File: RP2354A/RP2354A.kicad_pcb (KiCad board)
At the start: 2 copper layers, 40 x 80 mm, 66 parts, among them J101 USB4085-GF-A, J102 AudioJack2_SwitchT, J103 AudioJack2_SwitchT, J201 TC2030-NL, SW201 SW_Push_DPDT, U101 OPA365xxDBV, U201 RP2354A, U202 NCP1117-3.3_SOT223, U301 TAC5112, Y201 ABM8-272-T3

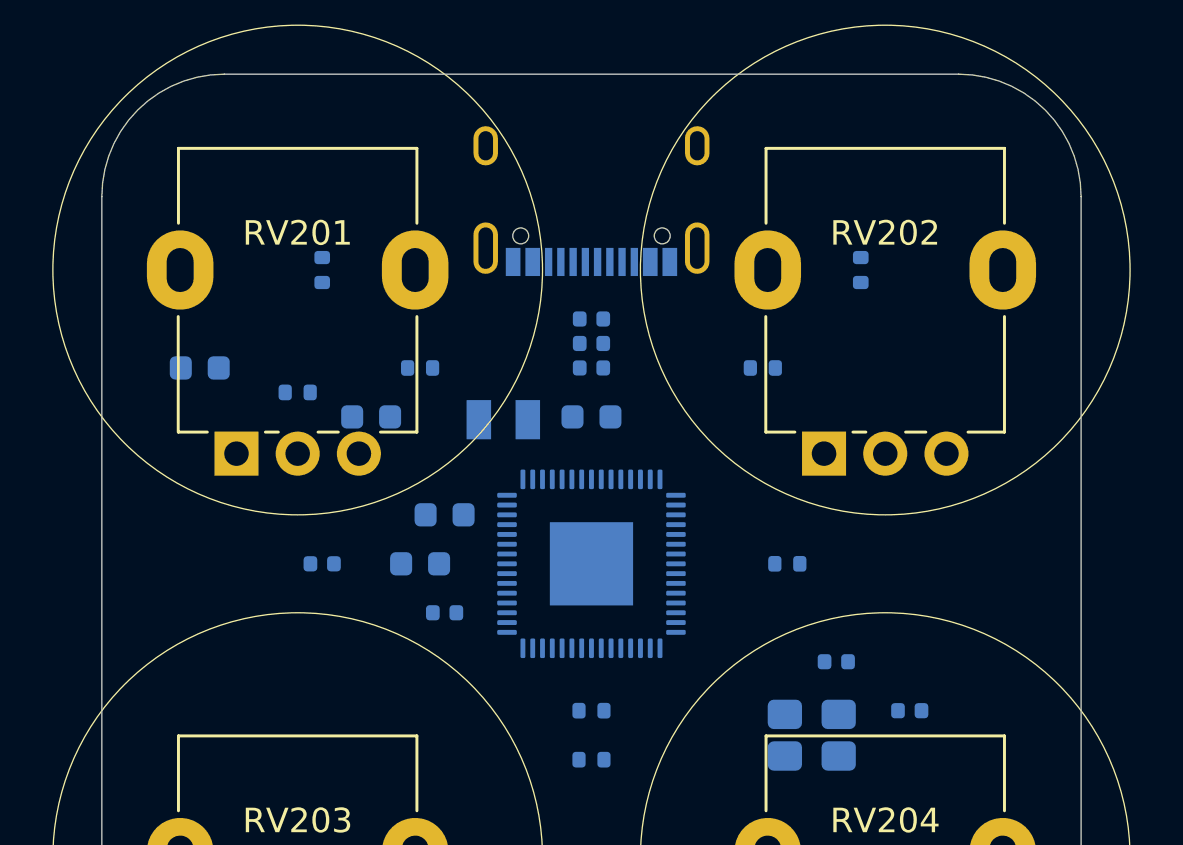
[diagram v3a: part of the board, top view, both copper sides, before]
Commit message: Replace two of the pots with basic ones without mounting pins
... for the most ridiculous of reasons: it frees up some board space
without altering the physical layout of knobs.

I can't replace all the pots with the basic ones, because the pots
themselves are physically bigger and won't fit, but this odd mix of
potentiometer types works, even if it's all kinds of odd.

Does this board need to be this form factor? No.  I could just move
things around.  But I like the size, I like the bigger 20mm diameter
knobs I'm planning on using, and I'm just doing this ridiculous thing
for fun in the first place, so having a fun form factor is part of it
all.

The ridiculous reason for having four knobs in the first place? That's
how many ADCs the RP2354A has. So this is all very random.

Next up: do a 4-layer stackup and actually start laying things out.

Signed-off-by: Linus Torvalds <torvalds@linux-foundation.org>
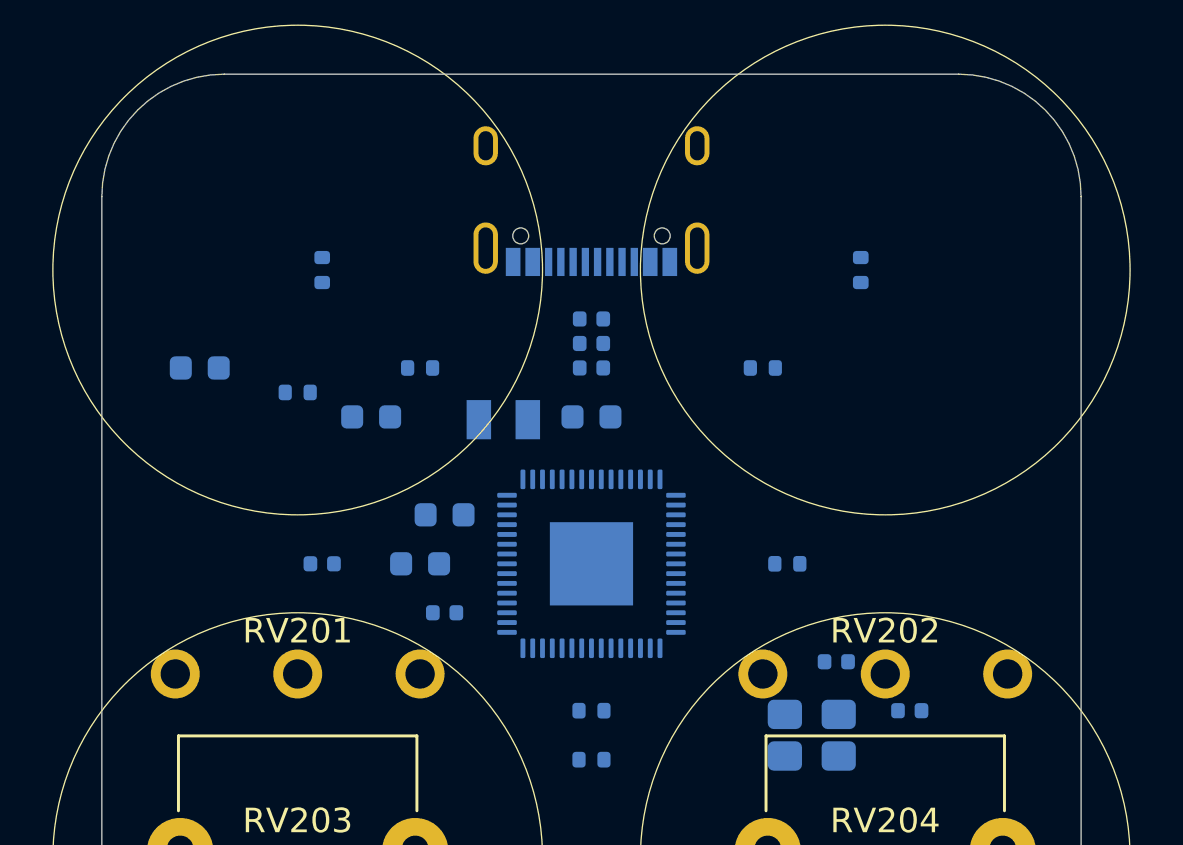
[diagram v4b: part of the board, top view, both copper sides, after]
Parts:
- RV201, RV202: footprint Mylib:Potentiometer_9mm_MP -> Mylib:Potentiometer-Basic

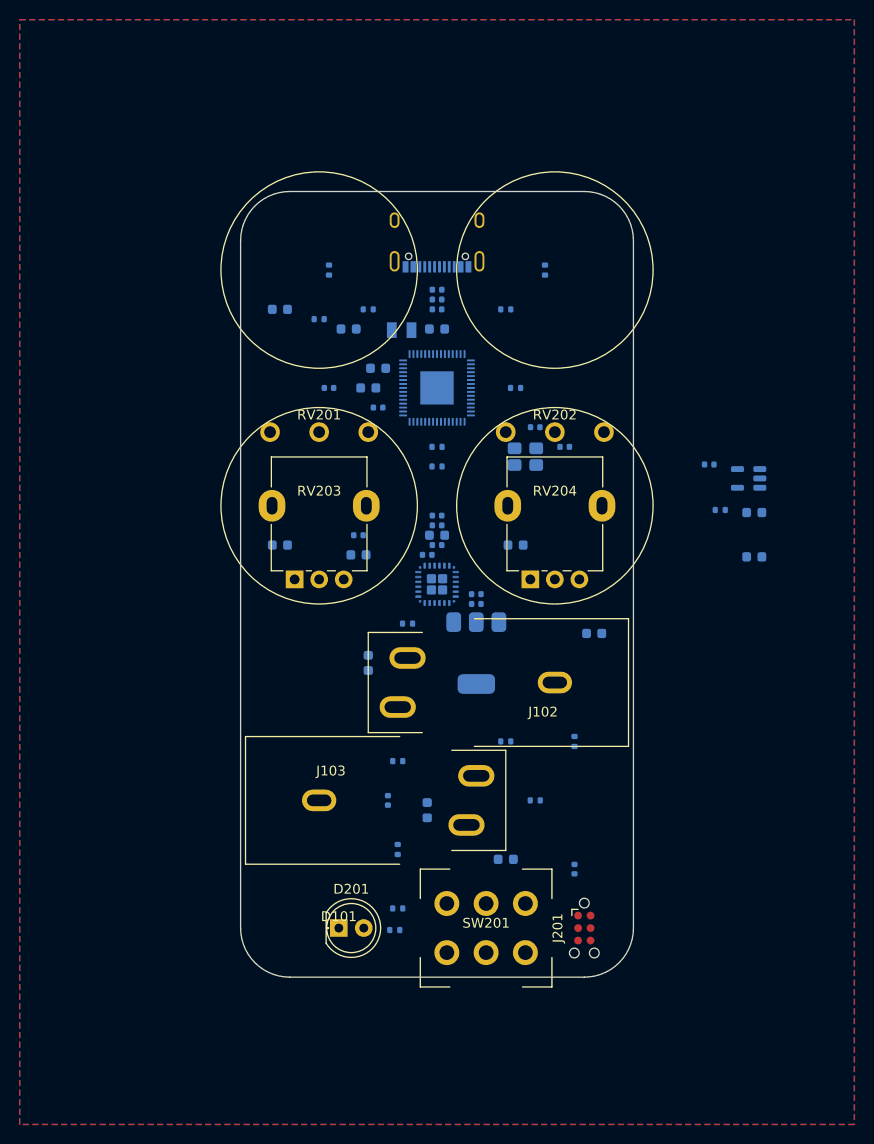
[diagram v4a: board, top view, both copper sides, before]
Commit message: rp2354: First stab at pcb layout
This is an insane 6-layer stackup, not because I need six layers
(although it does allow me to be even lazier than usual), but because I
want to use via-in-pad and at that point jlcpcb pretty much ends up
doing the whole precision 6-layer thing anyway.

The minimal RP2354A board makes do with just a simple two-layer stackup,
and I'm sure this could have been done that way too.  But with four
layers it's easy to just use one layer for the +1V1 zone and one for the
+3V3 zone under the RP2354A, and just bring things in with the vias.

This is all connected, but with some ERC noise. Mostly harmless (tm).

Also add JLCPCB part numbers to things, although I need to check them
all several times.

Signed-off-by: Linus Torvalds <torvalds@linux-foundation.org>
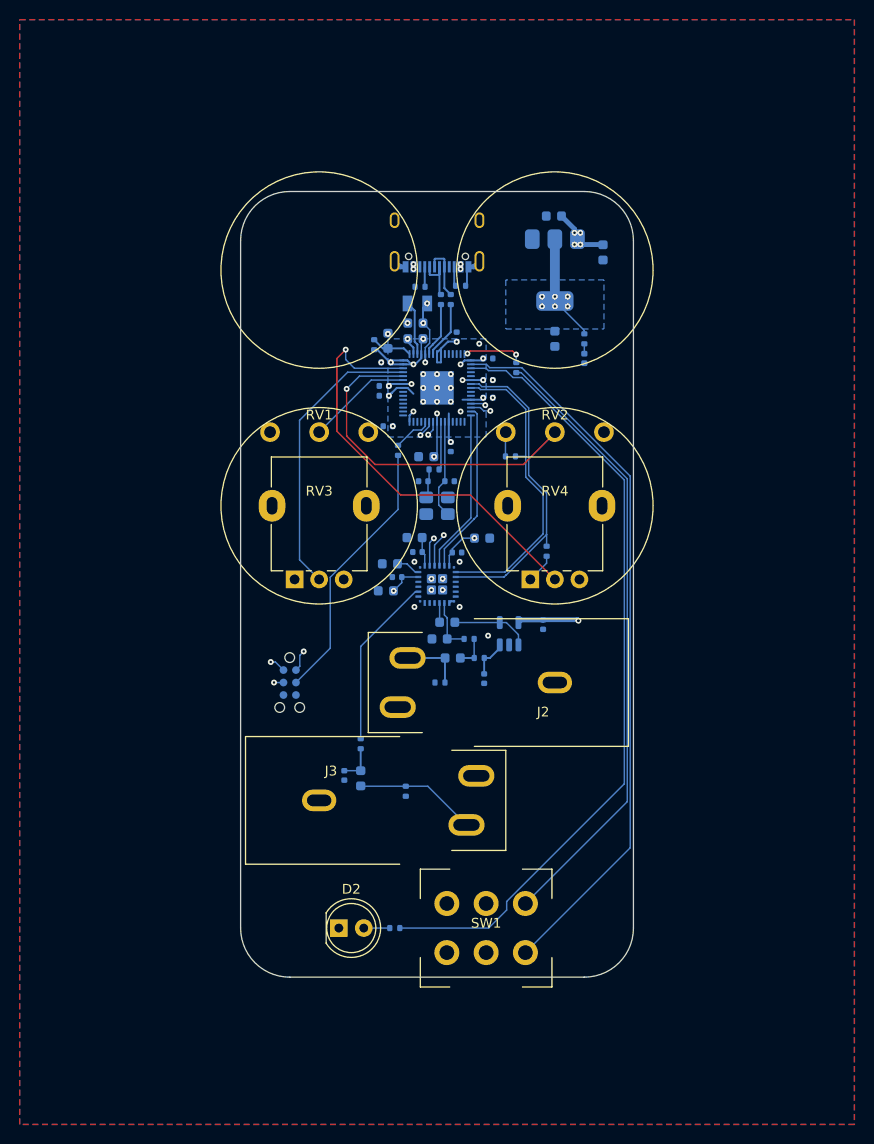
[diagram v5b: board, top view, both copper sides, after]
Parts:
- removed C216, C217: 10uF, Capacitor_SMD:C_0603_1608Metric
- removed U202: NCP1117-3.3_SOT223, Package_TO_SOT_SMD:SOT-223-3_TabPin2
- added C8: 10uF, Capacitor_SMD:C_0603_1608Metric, B.Cu at (111.9, 72.5)
- added C9: 10uF, Capacitor_SMD:C_0603_1608Metric, B.Cu at (112.0, 85.0)
- added U2: NCP1117-3.3_SOT223, Package_TO_SOT_SMD:SOT-223-3_TabPin2, B.Cu at (112.0, 78.0)
- D1: renamed from D101; moved to B.Cu
- J1: renamed from J101; value USB4085-GF-A -> TYPE-C16PIN
- J4: renamed from J201; moved to B.Cu
- R8: renamed from R106; value 5k1 -> 1k
- moved D1 63.2 mm to (115.0, 87.0), turned to 90 degrees
- moved R8 61.0 mm to (115.0, 85.0), turned to -90 degrees
- moved J4 39.1 mm to (85.0, 120.0)
- moved R11 38.3 mm to (96.0, 96.4), turned to 90 degrees
- moved R10 38.1 mm to (108.1, 87.9), turned to 90 degrees
- moved C32 33.1 mm to (100.3, 115.6)
- moved C3 30.6 mm to (116.9, 76.2), turned to 90 degrees
- moved U1 29.1 mm to (107.3, 115.0), turned to 90 degrees
- moved R2 28.7 mm to (103.3, 115.6), turned to 0 degrees
- moved C4 24.9 mm to (101.0, 113.9)
- moved C5 23.5 mm to (110.8, 114.1), turned to 90 degrees
- moved C10 23.3 mm to (97.8, 85.0)
- moved C17 22.3 mm to (94.6, 90.8)
- moved C26 21.8 mm to (104.6, 105.3)
- moved C2 21.5 mm to (104.8, 119.6), turned to -90 degrees
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- renumbered C101 to C1, C201 to C10, C202 to C11, C203 to C12, C204 to C13, C205 to C14, C206 to C15, C207 to C16, C208 to C17, C209 to C18, C210 to C19, C102 to C2, C211 to C20, C212 to C21, C213 to C22, C214 to C23, C215 to C24, C301 to C25, C302 to C26, C303 to C27, C304 to C28, C305 to C29, C103 to C3, C306 to C30, C307 to C31, C308 to C32, C104 to C4, C105 to C5, C106 to C6, C107 to C7, D201 to D2, J102 to J2, J103 to J3, L201 to L1, R101 to R1, R202 to R10, R203 to R11, R204 to R12, R205 to R13, R206 to R14, R207 to R15, R208 to R16, R209 to R17, R102 to R2, R103 to R3, R104 to R4, R105 to R5, R107 to R6, R108 to R7, R201 to R9, RV201 to RV1, RV202 to RV2, RV203 to RV3, RV204 to RV4, SW201 to SW1, U101 to U1, U201 to U3, U301 to U4, Y201 to Y1
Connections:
- R8 pad 1: VBUS -> +3V3
- U3 pad 18: TAC_GPIO1 -> unconnected-(U3-GPIO14-Pad18)
- U3 pad 19: TAC_GPIO2 -> unconnected-(U3-GPIO15-Pad19)
- U3 pad 27: TAC_GPO1 -> unconnected-(U3-GPIO16-Pad27)
- U3 pad 28: TAC_GPI1 -> unconnected-(U3-GPIO17-Pad28)
- U4 pad 10: TAC_GPIO2 -> unconnected-(U4-GPIO2-Pad10)
- U4 pad 11: TAC_GPO1 -> unconnected-(U4-GPO1-Pad11)
- U4 pad 12: TAC_GPI1 -> unconnected-(U4-GPI1-Pad12)
- U4 pad 9: TAC_GPIO1 -> unconnected-(U4-GPIO1-Pad9)
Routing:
- net /RPi/LED: track 0.00 -> 80.7 mm
- net /RPi/STOMP: track 0.00 -> 73.9 mm
- net /RPi/BOOTSEL: track 0.00 -> 63.3 mm
- net +3V3: track 0.00 -> 54.1 mm, vias 0 -> 22
- net VBUS: track 0.00 -> 53.4 mm, vias 0 -> 9
- net POT4: track 0.00 -> 44.4 mm, vias 0 -> 1
- net Net-(J4-SWCLK): track 0.00 -> 35.3 mm, vias 0 -> 2
- net POT2: track 0.00 -> 34.9 mm, vias 0 -> 1
- net Net-(J4-SWDIO): track 0.00 -> 34.2 mm, vias 0 -> 2
- net SDA: track 0.00 -> 32.8 mm
- net SCL: track 0.00 -> 31.5 mm
- net POT3: track 0.00 -> 29.6 mm
- net /RPi/NRST: track 0.00 -> 27.4 mm
- net FSYNC: track 0.00 -> 20.2 mm, vias 0 -> 2
- net BCLK: track 0.00 -> 20.2 mm, vias 0 -> 2
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- added copper zone on In2.Cu, net +1V1
- added copper zone on B.Cu, net +3V3
- added copper zone on In1.Cu, net +3V3
- added copper zone on In1.Cu, net VBUS
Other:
- copper layers 2 -> 6
